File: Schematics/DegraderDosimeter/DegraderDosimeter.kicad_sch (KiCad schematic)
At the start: 0 parts

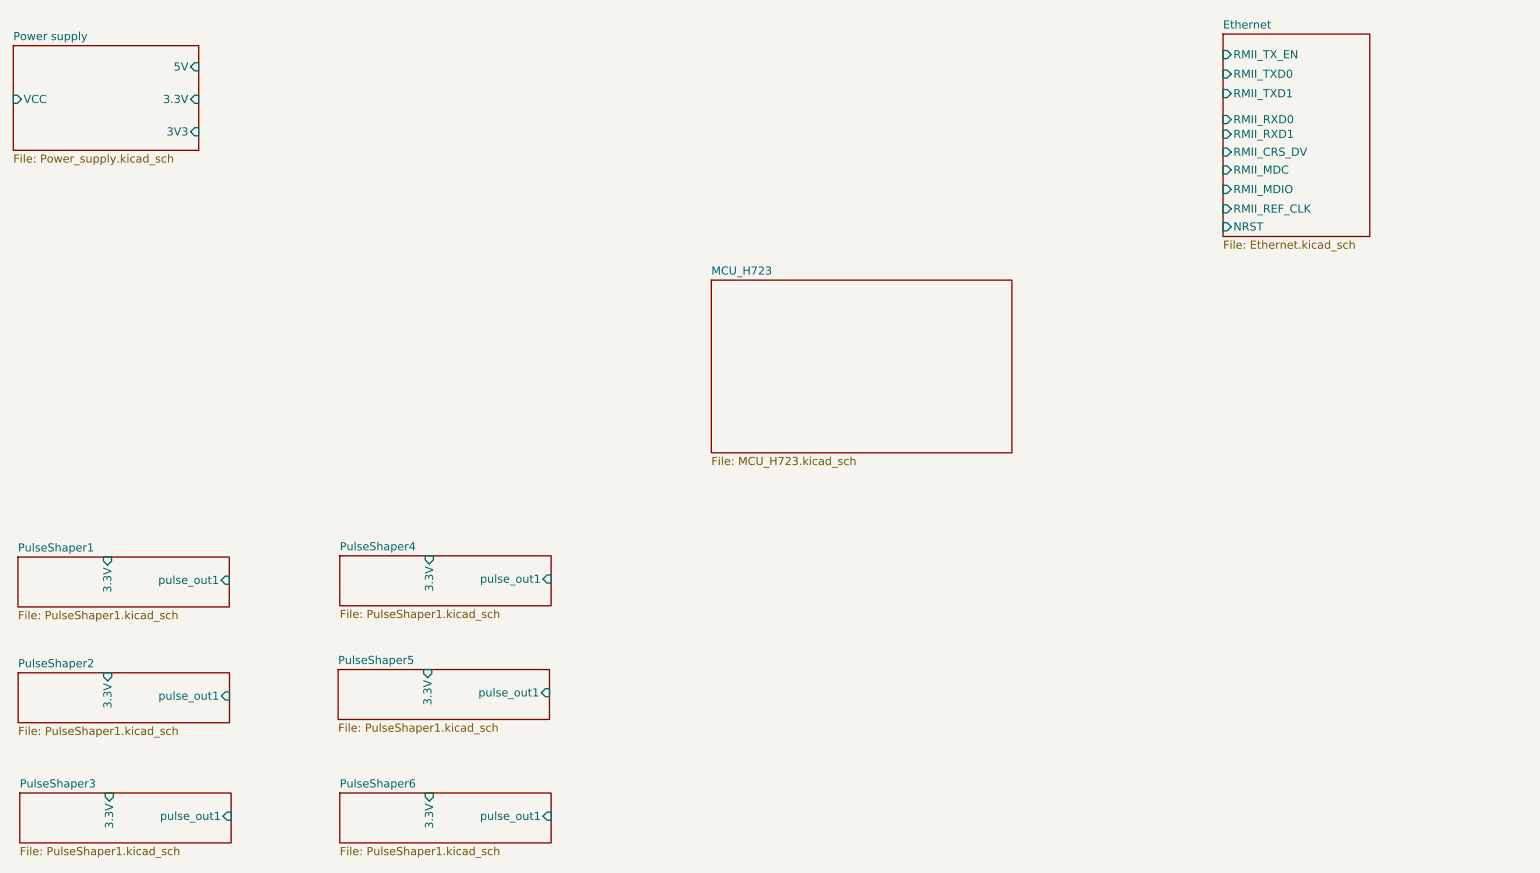
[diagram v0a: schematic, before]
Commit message: Fix broken hierarchical sheet references in DegraderDosimeter
The six PulseShaper sheet instances pointed at PulseShaper1.kicad_sch,
which was never committed and contains only a stray coax connector. The
populated pulse shaper circuit (2x ADA4891-2ARZ-R7, R28-R31, R33, C26,
C27, RV1, J2) lives in PulseShaper.kicad_sch, so repoint all six there.
Symbol instance data for all six sheet UUIDs already exists in that file,
so annotations resolve unchanged.

Also add Degrader.kicad_sch, which the top-level sheet references but was
likewise untracked, along with the A4988SETTR_T and L717HDE15P libraries
and the lib-table entries it needs to resolve.

Co-Authored-By: Claude Opus 5 <noreply@anthropic.com>
Claude-Session: https://claude.ai/code/session_01Ej9hevrS5JU2uwVi6UHQUS
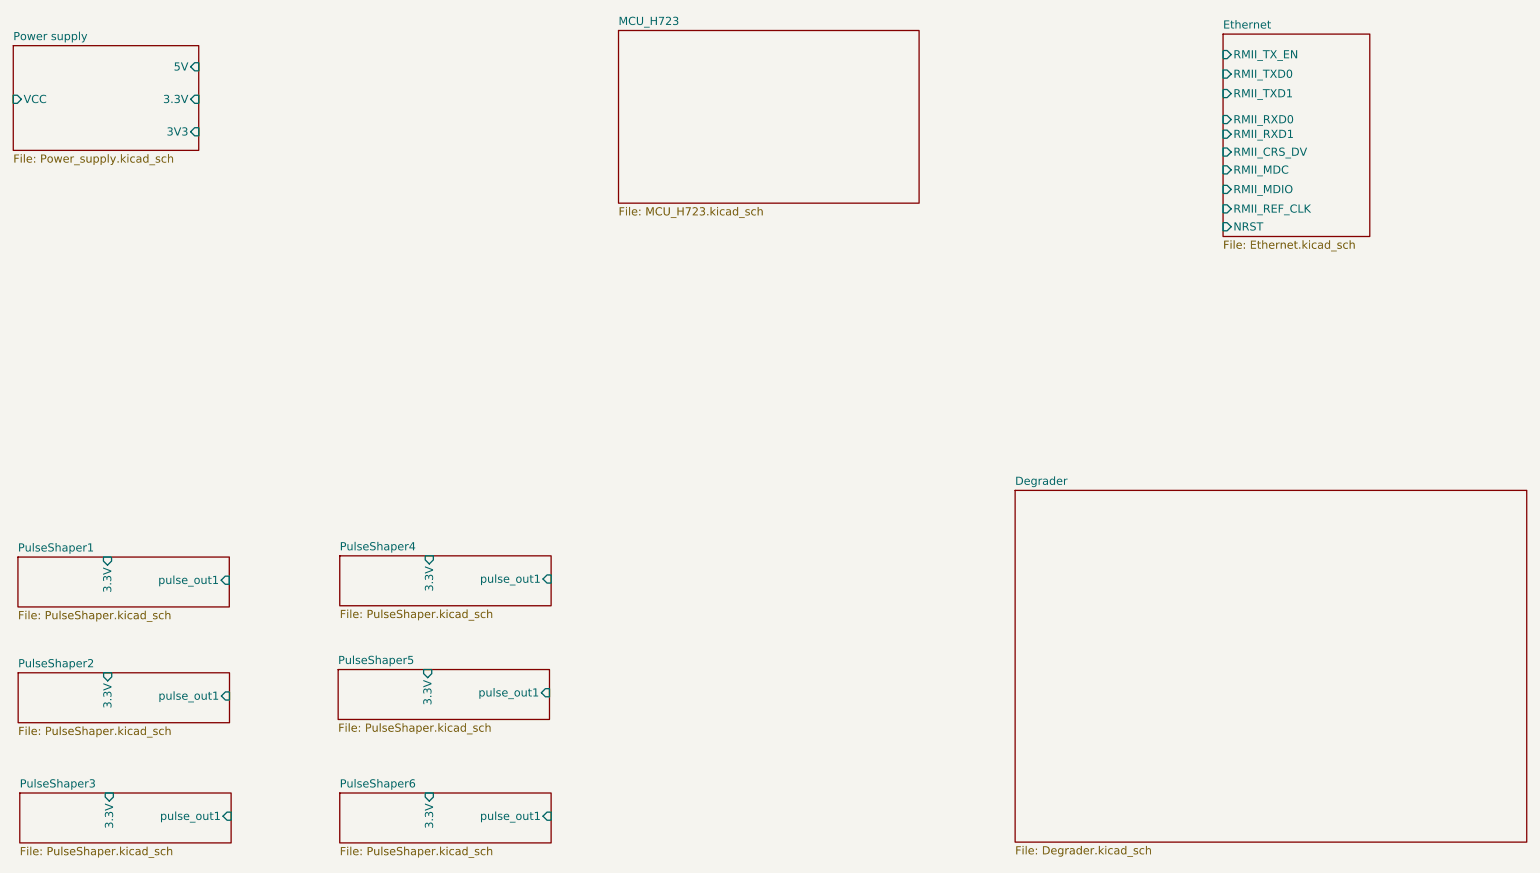
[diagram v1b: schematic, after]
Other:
- added sheet Degrader (Degrader.kicad_sch)
- sheet PulseShaper1: file PulseShaper1.kicad_sch -> PulseShaper.kicad_sch
- sheet PulseShaper2: file PulseShaper1.kicad_sch -> PulseShaper.kicad_sch
- sheet PulseShaper3: file PulseShaper1.kicad_sch -> PulseShaper.kicad_sch
- sheet PulseShaper4: file PulseShaper1.kicad_sch -> PulseShaper.kicad_sch
- sheet PulseShaper5: file PulseShaper1.kicad_sch -> PulseShaper.kicad_sch
- sheet PulseShaper6: file PulseShaper1.kicad_sch -> PulseShaper.kicad_sch
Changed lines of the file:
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@@
 			)
 		)
-		(property "Sheetfile" "PulseShaper1.kicad_sch"
+		(property "Sheetfile" "PulseShaper.kicad_sch"
 			(at 40.072 118.8106 0)
 			(show_name no)
@@
 			)
 		)
-		(property "Sheetfile" "PulseShaper1.kicad_sch"
+		(property "Sheetfile" "PulseShaper.kicad_sch"
 			(at 90.394 118.6246 0)
 			(show_name no)
@@
 			)
 		)
-		(property "Sheetfile" "PulseShaper1.kicad_sch"
+		(property "Sheetfile" "PulseShaper.kicad_sch"
 			(at 40.356 155.7086 0)
 			(show_name no)
@@
 	)
 	(sheet
-		(at 148.496 67.124)
+		(at 133.982 28.086)
 		(size 47 27)
 		(exclude_from_sim no)
@@
 		)
 		(property "Sheetname" "MCU_H723"
-			(at 148.496 66.4124 0)
+			(at 133.982 27.3744 0)
 			(show_name no)
 			(do_not_autoplace no)
@@
 		)
 		(property "Sheetfile" "MCU_H723.kicad_sch"
-			(at 148.496 94.7086 0)
+			(at 133.982 55.6706 0)
 			(show_name no)
 			(do_not_autoplace no)
@@
 				(path "/f3c83d46-b432-4960-ae55-27eb620ca6d0"
 					(page "3")
+				)
+			)
+		)
+	)
+	(sheet
+		(at 196 100)
+		(size 80 55)
+		(exclude_from_sim no)
+		(in_bom yes)
+		(on_board yes)
+		(dnp no)
+		(fields_autoplaced yes)
+		(stroke
+			(width 0.1524)
+			(type solid)
+		)
+		(fill
+			(color 0 0 0 0)
+		)
+		(property "Sheetname" "Degrader"
+			(at 196 99.2884 0)
+			(show_name no)
+			(do_not_autoplace no)
+			(effects
+				(font
+					(size 1.27 1.27)
+				)
+				(justify left bottom)
+			)
+		)
+		(property "Sheetfile" "Degrader.kicad_sch"
+			(at 196 155.5846 0)
+			(show_name no)
+			(do_not_autoplace no)
+			(effects
+				(font
+					(size 1.27 1.27)
+				)
+				(justify left top)
+			)
+		)
+		(instances
+			(project "DegraderDosimeter"
+				(path "/f3c83d46-b432-4960-ae55-27eb620ca6d0"
+					(page "11")
 				)
 			)
@@
 			)
 		)
-		(property "Sheetfile" "PulseShaper1.kicad_sch"
+		(property "Sheetfile" "PulseShaper.kicad_sch"
 			(at 90.394 155.7086 0)
 			(show_name no)
@@
 			)
 		)
-		(property "Sheetfile" "PulseShaper1.kicad_sch"
+		(property "Sheetfile" "PulseShaper.kicad_sch"
 			(at 40.102 136.9126 0)
 			(show_name no)
@@
 			)
 		)
-		(property "Sheetfile" "PulseShaper1.kicad_sch"
+		(property "Sheetfile" "PulseShaper.kicad_sch"
 			(at 90.14 136.4046 0)
 			(show_name no)
